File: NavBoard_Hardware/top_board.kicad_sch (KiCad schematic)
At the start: 8 parts, among them J6 01x03, J7 01x03, J8 Conn_02x16_Separate, J9 6 Pin Molex Micro-Fit

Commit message: Annotated schematic pages
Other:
- company: (none) -> Thomas Francois, Missouri S&T Mars Rover Design Team
- title: (none) -> MRDT NavBoard - Top Board
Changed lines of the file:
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@@
 (kicad_sch (version 20211123) (generator eeschema)
   (paper "A4")
+  (title_block
+    (title "MRDT NavBoard - Top Board")
+    (rev "1, 2023")
+    (company "Thomas Francois, Missouri S&T Mars Rover Design Team")
+    (comment 1 "Topmost Teensy module")
+    (comment 2 "Contains Molex Micro-Fit for GPS, and 2 accelerometers")
+  )
   (junction (at 168.275 94.615) (diameter 0) (color 0 0 0 0)
   )

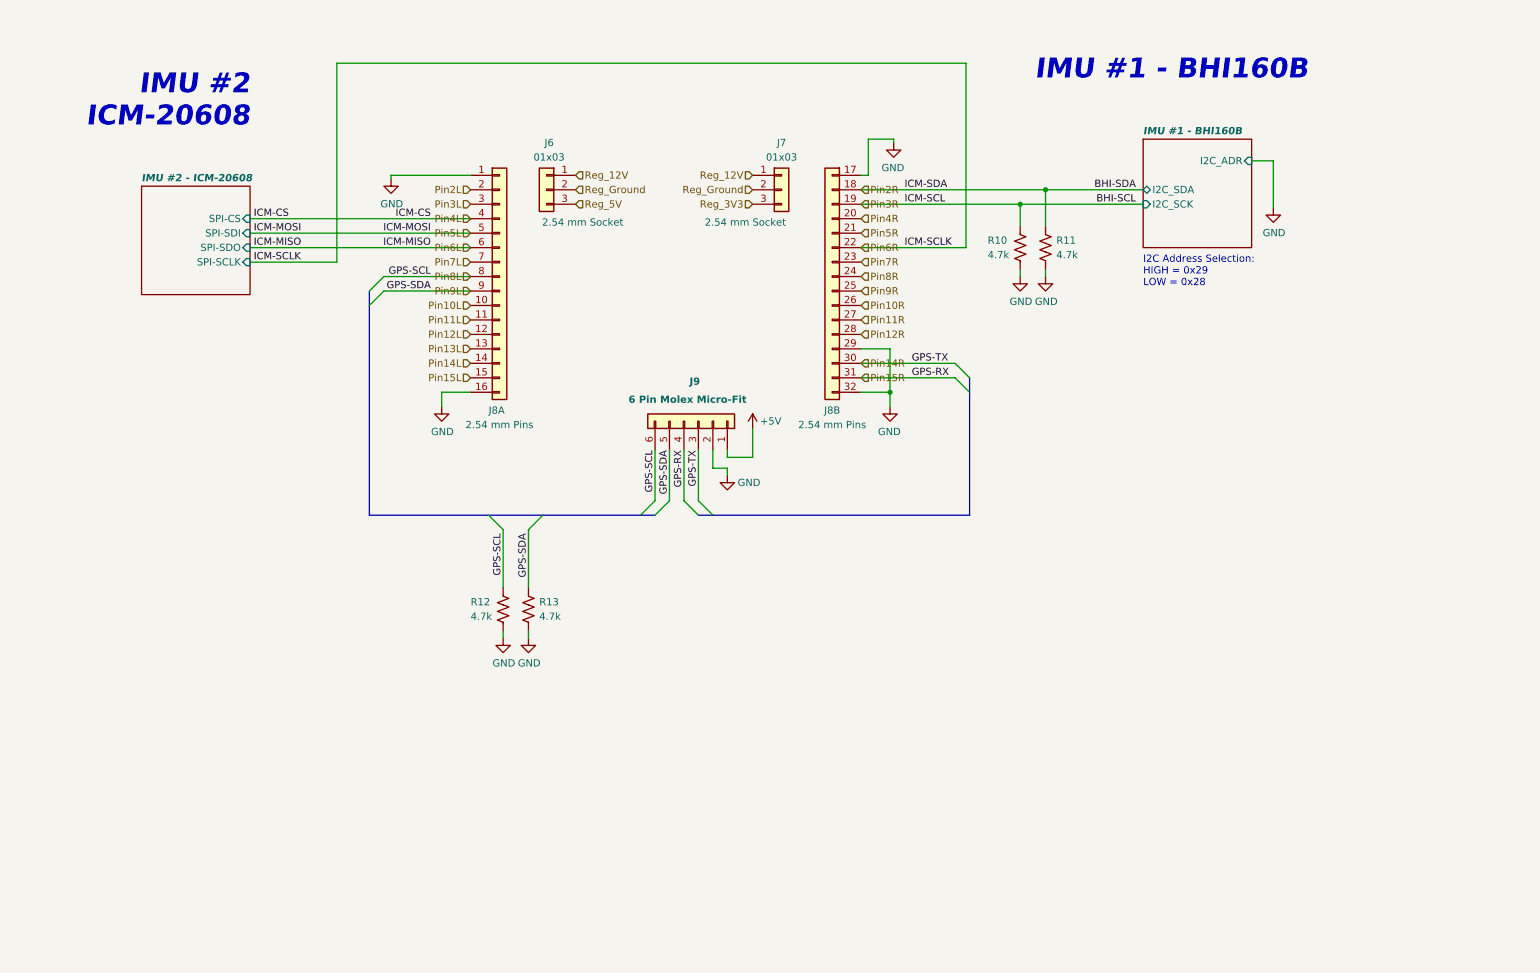
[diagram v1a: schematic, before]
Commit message: Rearranged schematic
I realize now that this is a dumb idea...
Going to redesign the board so the teensy just sits on top
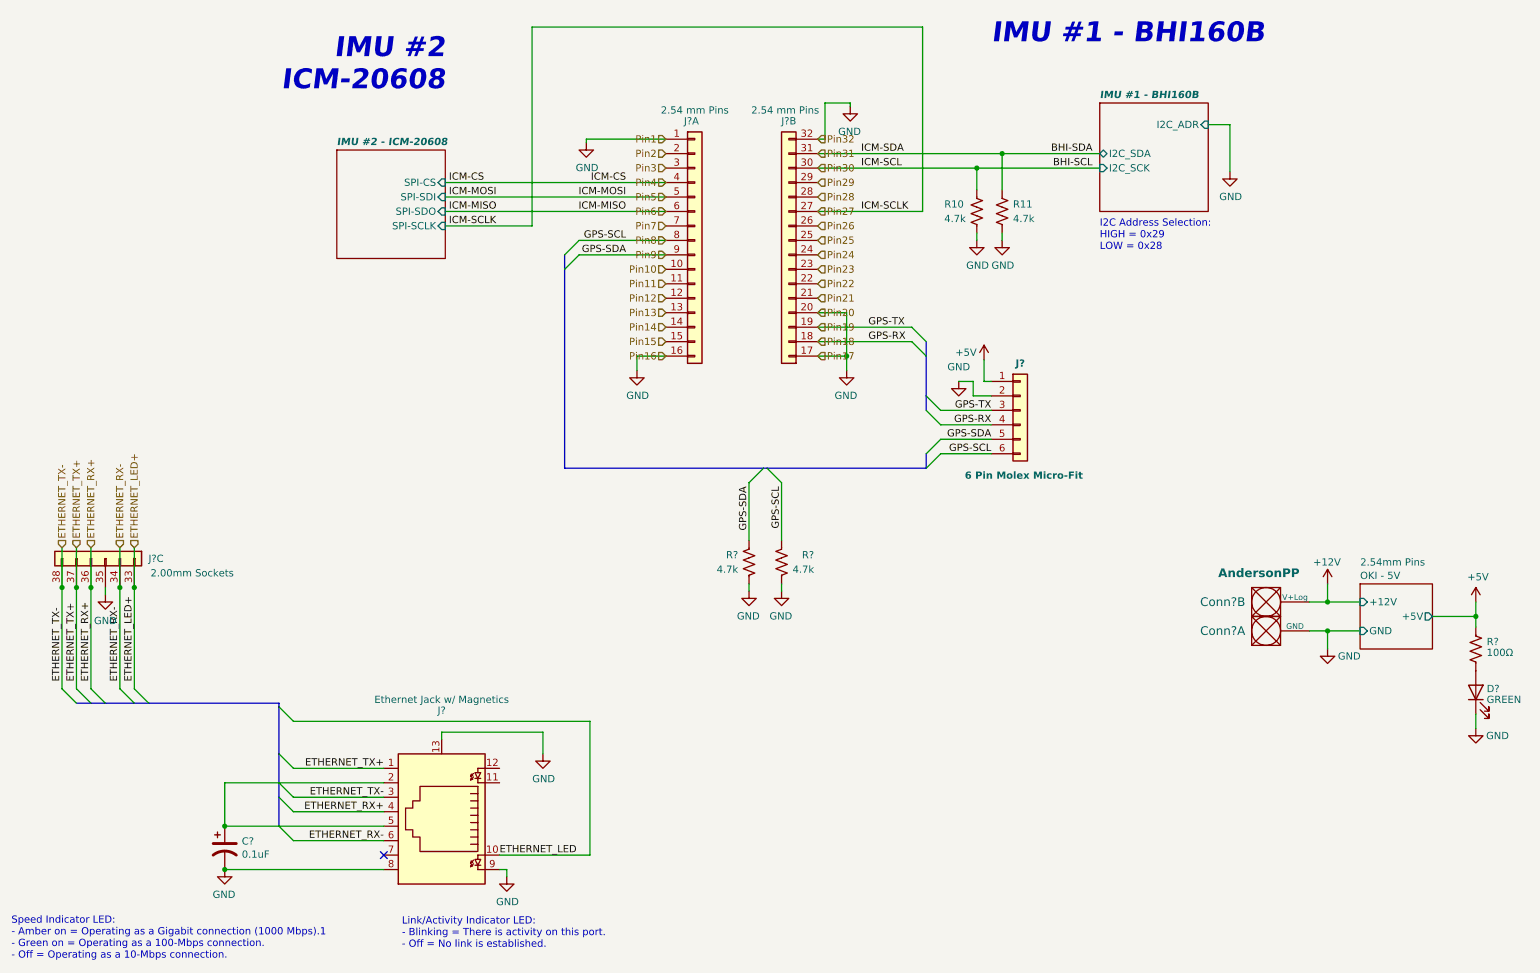
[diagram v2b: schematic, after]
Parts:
- removed J6, J7: 01x03, Connector_PinSocket_2.54mm:PinSocket_1x03_P2.54mm_Vertical, symbol Connector_Generic:Conn_01x03
- added C?: 0.1uF, Capacitor_SMD:C_0603_1608Metric_Pad1.08x0.95mm_HandSolder, symbol Device:C_Polarized_US
- added Conn? (x2): AndersonPP, MRDT_Connectors:Anderson_2_Vertical_Sidy_by_Side, symbol MRDT_Connectors:AndersonPP
- added D?: GREEN, LED_SMD:LED_0603_1608Metric_Pad1.05x0.95mm_HandSolder, symbol Device:LED
- added J?: Ethernet Jack w/ Magnetics, Connector_RJ:RJ45_Cetus_J1B1211CCD_Horizontal, symbol Connector:8P8C_LED_Shielded
- added J?: Conn_02x16_Separate_1, Nav_Board:PinSocket_2x16_P2.54mm_Vertical_Nav_Board, symbol Nav_Board:Conn_02x16_Separate_1
- added R?: 100Ω, Resistor_SMD:R_0603_1608Metric_Pad0.98x0.95mm_HandSolder, symbol Device:R_US
- J? (x2): renamed from J8; value Conn_02x16_Separate -> Conn_02x16_Separate_1; symbol Nav_Board:Conn_02x16_Separate -> Nav_Board:Conn_02x16_Separate_1
- renumbered J9 to J?, R12 to R?, R13 to R?
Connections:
- net Pin4R is gone; now on net GND: J?.20
- net +5V: now also R?.1
- net GND: now also C?.2, Conn?.1 (GND), D?.1 (K), J?.13, J?.35, J?.8, J?.9; no longer J?.29
- net Pin10L renamed Pin10
- net Pin10R renamed Pin26
- net Pin11L renamed Pin11
- net Pin11R renamed Pin27
- net Pin12L renamed Pin12
- net Pin12R renamed Pin28
- net Pin13L renamed Pin13
- net Pin14L renamed Pin14
- net Pin14R renamed Pin19
- net Pin19: now also J?.19; no longer J?.30
- net Pin15L renamed Pin15
- net Pin15R renamed Pin18
- net Pin18: now also J?.18; no longer J?.31
- net Pin2L renamed Pin2
- net Pin2R renamed Pin31
- net Pin31: now also J?.31; no longer J?.18
- net Pin3L renamed Pin3
- net Pin3R renamed Pin30
- net Pin30: now also J?.30; no longer J?.19
- net Pin4L renamed Pin4
- net Pin5L renamed Pin5
- net Pin5R renamed Pin21
- net Pin6L renamed Pin6
- net Pin6R renamed Pin22
- net Pin7L renamed Pin7
- net Pin7R renamed Pin23
- net Pin8L renamed Pin8
- net Pin8R renamed Pin24
- net Pin9L renamed Pin9
- net Pin9R renamed Pin25
- new net: C?.1, J?.2, J?.5
- new net: D?.2 (A), R?.2
- new net +12V: Conn?.2 (V+Log)
- new net ETHERNET_LED: J?.10
- new net ETHERNET_LED+: J?.33
- new net ETHERNET_RX+: J?.36, J?.4
- new net ETHERNET_RX-: J?.34, J?.6
- new net ETHERNET_TX+: J?.1, J?.37
- new net ETHERNET_TX-: J?.3, J?.38
- new net Pin29: J?.29
- no-connect marks 0 -> 1
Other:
- added sheet OKI - 5V (component_sheets\OKI-5V.kicad_sch)
- note added: "Link/Activity Indicator LED: - Blinking = There is activity on this port. - Off = No link is established."
- note added: "Speed Indicator LED: - Amber on = Operating as a Gigabit connection (1000 Mbps).1 - Green on = Operating as a 100-Mbps connection. - Off = Operating as a 10-Mbps connection."
- moved on the sheet: J?, J?A, J?B, R10, R11, R?

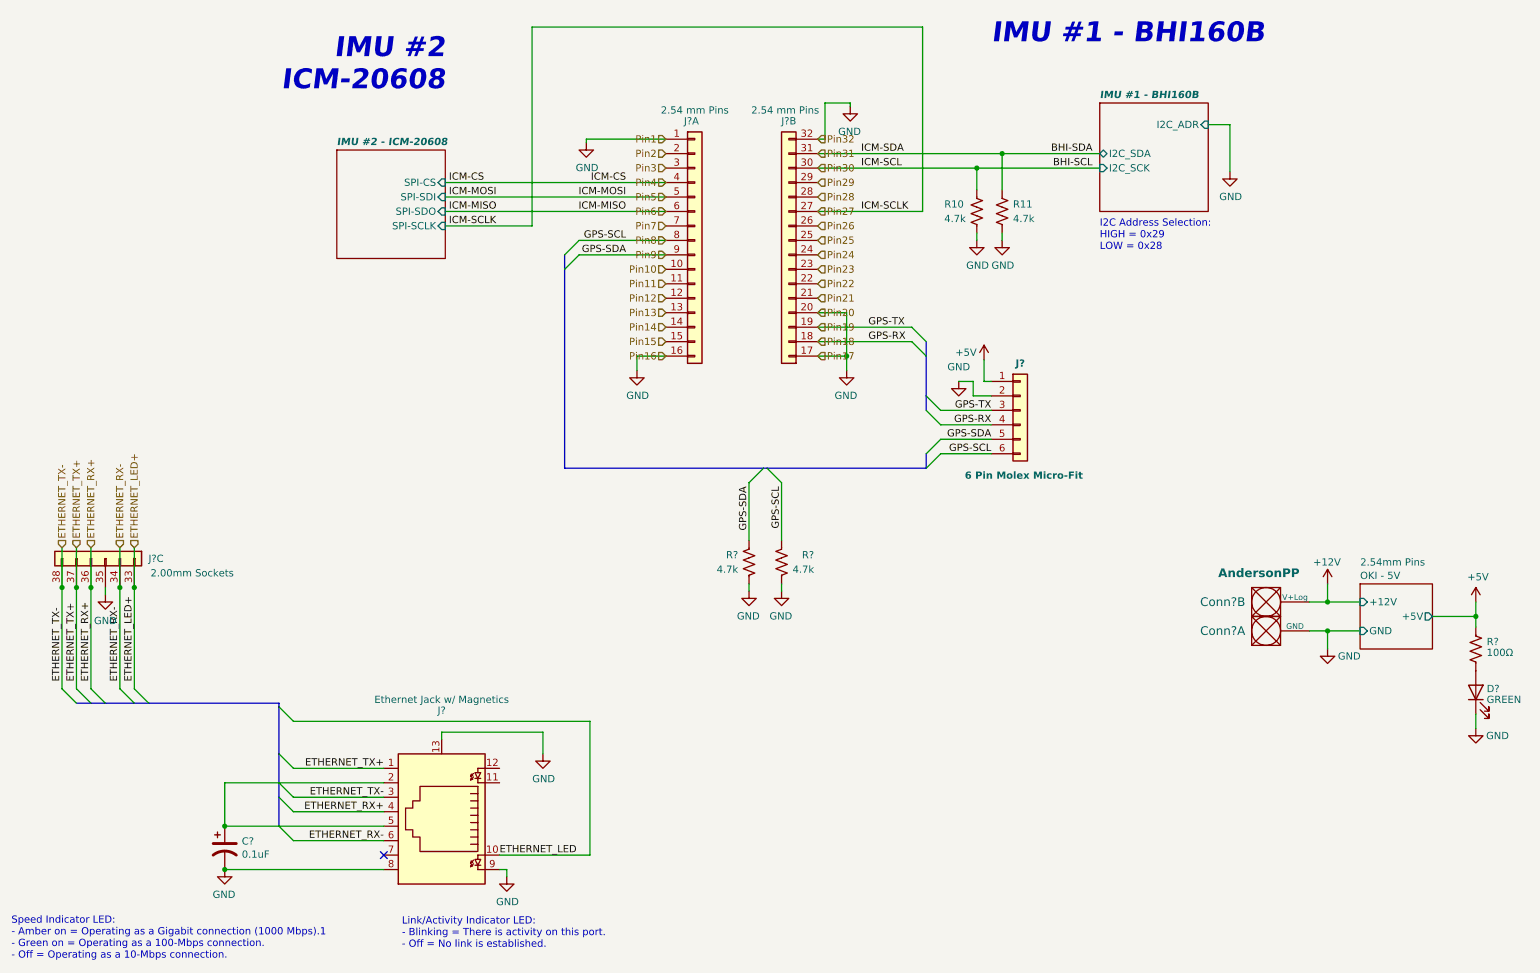
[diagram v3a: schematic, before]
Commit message: Realized this could all fit on a single board
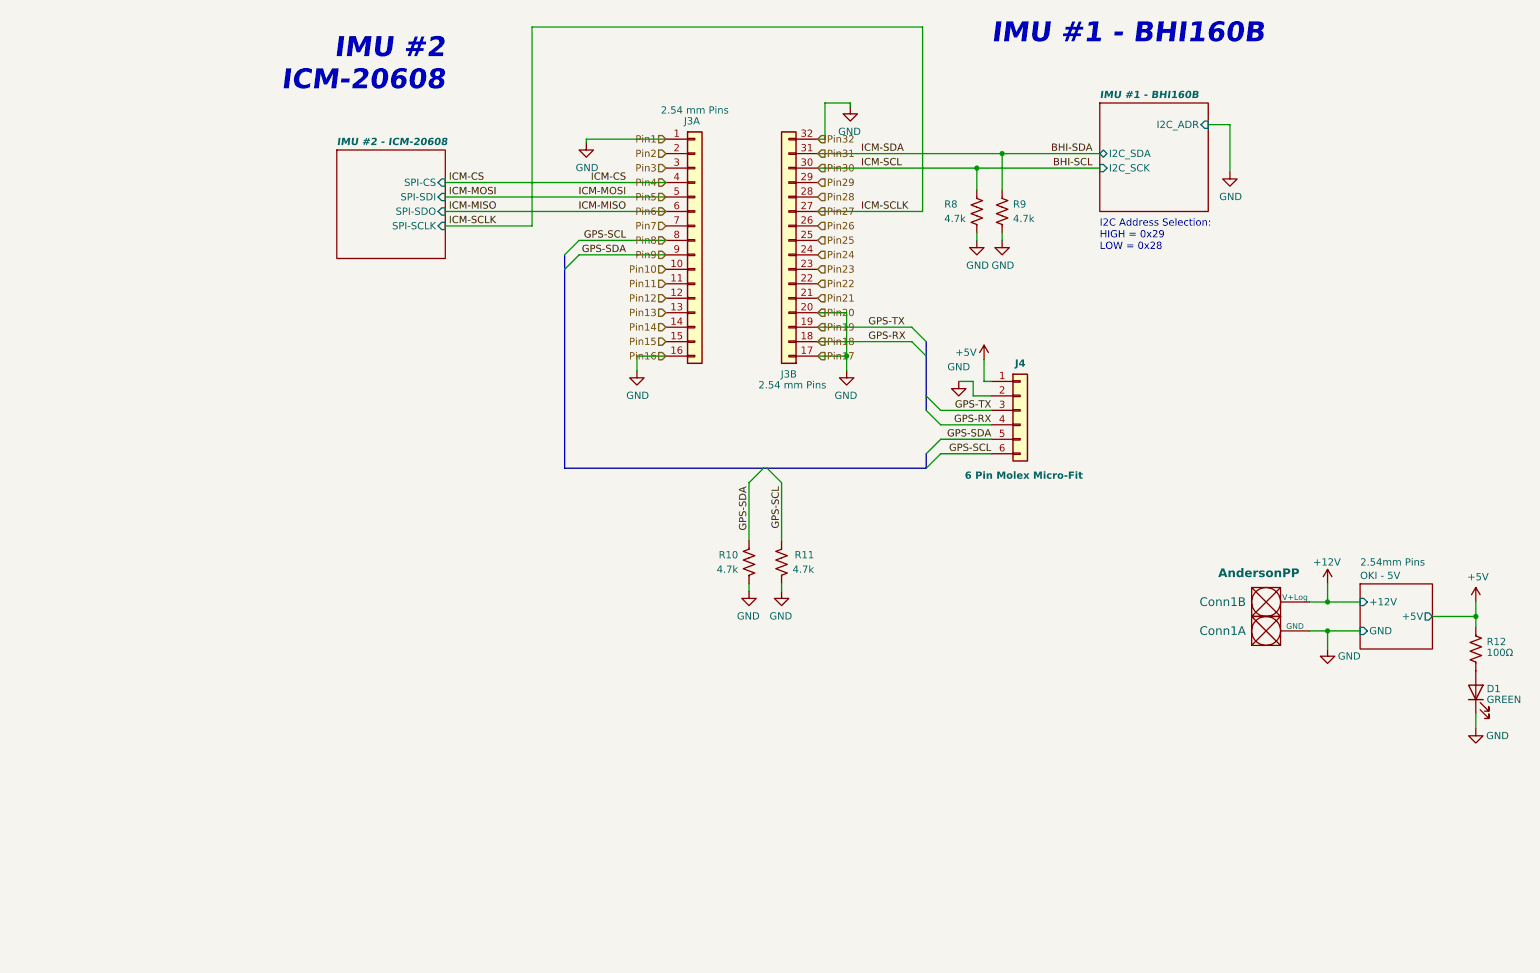
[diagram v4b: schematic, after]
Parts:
- removed C?: 0.1uF, Capacitor_SMD:C_0603_1608Metric_Pad1.08x0.95mm_HandSolder, symbol Device:C_Polarized_US
- removed J?: Ethernet Jack w/ Magnetics, Connector_RJ:RJ45_Cetus_J1B1211CCD_Horizontal, symbol Connector:8P8C_LED_Shielded
- removed J?: Conn_02x16_Separate_1, Nav_Board:PinSocket_2x16_P2.54mm_Vertical_Nav_Board, symbol Nav_Board:Conn_02x16_Separate_1
- gave numbers to parts that had none: 7
- renumbered R10 to R8, R11 to R9
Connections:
- no-connect marks 1 -> 0
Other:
- note removed: "Link/Activity Indicator LED: - Blinking = There is activity on this port. - Off = No link is established."
- note removed: "Speed Indicator LED: - Amber on = Operating as a Gigabit connection (1000 Mbps).1 - Green on = Operating as a 100-Mbps connection. - Off = Operating as a 10-Mbps connection."
